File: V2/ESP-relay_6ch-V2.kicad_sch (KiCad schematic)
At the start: 103 parts, among them J1 24VDC, J2 24V INPUTS, J3 OUT1, J4 OUT1, J5 OUT1, J6 OUT1, J7 OUT1, J8 OUT1, K1 G5PZ-1A, K2 G5PZ-1A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

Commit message: footprint updates
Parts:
- C1, C2: symbol Device:CP1_Small -> Device:C_Polarized_Small_US
- U4, U5, U6, U7, U8, U9: footprint Tales:SMDIP-4_W9.53mm -> Package_DIP:SMDIP-4_W9.53mm
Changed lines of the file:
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@@
       (effects (font (size 1.27 1.27) italic) (justify left) hide)
     )
-    (property "Datasheet" "~" (id 3) (at 203.2 30.48 0)
+    (property "Datasheet" "http://www.st.com/content/ccc/resource/technical/document/datasheet/41/4f/b3/b0/12/d4/47/88/CD00000444.pdf/files/CD00000444.pdf/jcr:content/translations/en.CD00000444.pdf" (id 3) (at 203.2 30.48 0)
       (effects (font (size 1.27 1.27)) hide)
     )
@@
       (effects (font (size 1.27 1.27)) hide)
     )
-    (property "Datasheet" "~" (id 3) (at 312.42 72.39 0)
+    (property "Datasheet" "https://wiki.wemos.cc/products:d1:d1_mini#documentation" (id 3) (at 312.42 72.39 0)
       (effects (font (size 1.27 1.27)) hide)
     )
@@
       (effects (font (size 1.27 1.27)) (justify left) hide)
     )
-    (property "Datasheet" "~" (id 3) (at 349.25 93.98 0)
+    (property "Datasheet" "https://www.omron.com/ecb/products/pdf/en-g5q.pdf" (id 3) (at 349.25 93.98 0)
       (effects (font (size 1.27 1.27)) hide)
     )
@@
       (effects (font (size 1.27 1.27)) (justify left) hide)
     )
-    (property "Datasheet" "~" (id 3) (at 232.41 147.32 0)
+    (property "Datasheet" "https://www.omron.com/ecb/products/pdf/en-g5q.pdf" (id 3) (at 232.41 147.32 0)
       (effects (font (size 1.27 1.27)) hide)
     )
@@
       (effects (font (size 1.27 1.27)) (justify left) hide)
     )
-    (property "Datasheet" "~" (id 3) (at 349.25 147.32 0)
+    (property "Datasheet" "https://www.omron.com/ecb/products/pdf/en-g5q.pdf" (id 3) (at 349.25 147.32 0)
       (effects (font (size 1.27 1.27)) hide)
     )
@@
       (effects (font (size 1.27 1.27)) (justify left) hide)
     )
-    (property "Datasheet" "~" (id 3) (at 232.41 200.66 0)
+    (property "Datasheet" "https://www.omron.com/ecb/products/pdf/en-g5q.pdf" (id 3) (at 232.41 200.66 0)
       (effects (font (size 1.27 1.27)) hide)
     )
@@
       (effects (font (size 1.27 1.27)) (justify left) hide)
     )
-    (property "Datasheet" "~" (id 3) (at 349.25 200.66 0)
+    (property "Datasheet" "https://www.omron.com/ecb/products/pdf/en-g5q.pdf" (id 3) (at 349.25 200.66 0)
       (effects (font (size 1.27 1.27)) hide)
     )
@@
       (effects (font (size 1.27 1.27)) (justify left) hide)
     )
-    (property "Datasheet" "~" (id 3) (at 232.41 93.98 0)
+    (property "Datasheet" "https://www.omron.com/ecb/products/pdf/en-g5q.pdf" (id 3) (at 232.41 93.98 0)
       (effects (font (size 1.27 1.27)) hide)
     )
@@
     (pin "4")
   )
-  (symbol (lib_id "Device:CP1_Small") (at 48.26 71.12 0) (unit 1)
+  (symbol (lib_id "Device:C_Polarized_Small_US") (at 48.26 71.12 0) (unit 1)
     (in_bom yes) (on_board yes)
     (property "Reference" "C2" (id 0) (at 50.8 68.58 0)
@@
     (pin "1")
   )
-  (symbol (lib_id "Device:CP1_Small") (at 22.86 71.12 0) (unit 1)
+  (symbol (lib_id "Device:C_Polarized_Small_US") (at 22.86 71.12 0) (unit 1)
     (in_bom yes) (on_board yes)
     (property "Reference" "C1" (id 0) (at 25.4 68.58 0)
@@
     (property "Reference" "U6" (id 0) (at 120.65 151.13 0))
     (property "Value" "LTV-817S" (id 1) (at 120.65 153.67 0))
-    (property "Footprint" "Tales:SMDIP-4_W9.53mm" (id 2) (at 120.65 170.18 0)
+    (property "Footprint" "Package_DIP:SMDIP-4_W9.53mm" (id 2) (at 120.65 170.18 0)
       (effects (font (size 1.27 1.27)) hide)
     )
-    (property "Datasheet" "~" (id 3) (at 111.76 154.94 0)
+    (property "Datasheet" "http://www.us.liteon.com/downloads/LTV-817-827-847.PDF" (id 3) (at 111.76 154.94 0)
       (effects (font (size 1.27 1.27)) hide)
     )
@@
     (property "Reference" "U7" (id 0) (at 120.65 172.72 0))
     (property "Value" "LTV-817S" (id 1) (at 120.65 175.26 0))
-    (property "Footprint" "Tales:SMDIP-4_W9.53mm" (id 2) (at 120.65 191.77 0)
+    (property "Footprint" "Package_DIP:SMDIP-4_W9.53mm" (id 2) (at 120.65 191.77 0)
       (effects (font (size 1.27 1.27)) hide)
     )
-    (property "Datasheet" "~" (id 3) (at 111.76 176.53 0)
+    (property "Datasheet" "http://www.us.liteon.com/downloads/LTV-817-827-847.PDF" (id 3) (at 111.76 176.53 0)
       (effects (font (size 1.27 1.27)) hide)
     )
@@
     (property "Reference" "U5" (id 0) (at 120.65 129.54 0))
     (property "Value" "LTV-817S" (id 1) (at 120.65 132.08 0))
-    (property "Footprint" "Tales:SMDIP-4_W9.53mm" (id 2) (at 120.65 148.59 0)
+    (property "Footprint" "Package_DIP:SMDIP-4_W9.53mm" (id 2) (at 120.65 148.59 0)
       (effects (font (size 1.27 1.27)) hide)
     )
-    (property "Datasheet" "~" (id 3) (at 111.76 133.35 0)
+    (property "Datasheet" "http://www.us.liteon.com/downloads/LTV-817-827-847.PDF" (id 3) (at 111.76 133.35 0)
       (effects (font (size 1.27 1.27)) hide)
     )
@@
     (property "Reference" "U9" (id 0) (at 120.65 215.9 0))
     (property "Value" "LTV-817S" (id 1) (at 120.65 218.44 0))
-    (property "Footprint" "Tales:SMDIP-4_W9.53mm" (id 2) (at 120.65 234.95 0)
+    (property "Footprint" "Package_DIP:SMDIP-4_W9.53mm" (id 2) (at 120.65 234.95 0)
       (effects (font (size 1.27 1.27)) hide)
     )
-    (property "Datasheet" "~" (id 3) (at 111.76 219.71 0)
+    (property "Datasheet" "http://www.us.liteon.com/downloads/LTV-817-827-847.PDF" (id 3) (at 111.76 219.71 0)
       (effects (font (size 1.27 1.27)) hide)
     )
@@
   (symbol (lib_id "power:GNDREF") (at 176.53 49.53 0) (unit 1)
     (in_bom yes) (on_board yes)
-    (property "Reference" "#PWR?" (id 0) (at 176.53 55.88 0)
+    (property "Reference" "#PWR0108" (id 0) (at 176.53 55.88 0)
       (effects (font (size 1.27 1.27)) hide)
     )
@@
     (property "Reference" "U8" (id 0) (at 120.65 194.31 0))
     (property "Value" "LTV-817S" (id 1) (at 120.65 196.85 0))
-    (property "Footprint" "Tales:SMDIP-4_W9.53mm" (id 2) (at 120.65 213.36 0)
+    (property "Footprint" "Package_DIP:SMDIP-4_W9.53mm" (id 2) (at 120.65 213.36 0)
       (effects (font (size 1.27 1.27)) hide)
     )
-    (property "Datasheet" "~" (id 3) (at 111.76 198.12 0)
+    (property "Datasheet" "http://www.us.liteon.com/downloads/LTV-817-827-847.PDF" (id 3) (at 111.76 198.12 0)
       (effects (font (size 1.27 1.27)) hide)
     )
@@
     (property "Reference" "U4" (id 0) (at 120.65 107.95 0))
     (property "Value" "LTV-817S" (id 1) (at 120.65 110.49 0))
-    (property "Footprint" "Tales:SMDIP-4_W9.53mm" (id 2) (at 120.65 127 0)
+    (property "Footprint" "Package_DIP:SMDIP-4_W9.53mm" (id 2) (at 120.65 127 0)
       (effects (font (size 1.27 1.27)) hide)
     )
-    (property "Datasheet" "~" (id 3) (at 111.76 111.76 0)
+    (property "Datasheet" "http://www.us.liteon.com/downloads/LTV-817-827-847.PDF" (id 3) (at 111.76 111.76 0)
       (effects (font (size 1.27 1.27)) hide)
     )
@@
     )
     (path "/9385be33-d48d-4257-8c07-24842288edd5"
-      (reference "#PWR?") (unit 1) (value "GNDREF") (footprint "")
+      (reference "#PWR0108") (unit 1) (value "GNDREF") (footprint "")
     )
     (path "/00000000-0000-0000-0000-000062418b8f"
@@
     )
     (path "/e41c8ba8-d546-4f8b-b36a-c7995cebe79c"
-      (reference "U4") (unit 1) (value "LTV-817S") (footprint "Tales:SMDIP-4_W9.53mm")
+      (reference "U4") (unit 1) (value "LTV-817S") (footprint "Package_DIP:SMDIP-4_W9.53mm")
     )
     (path "/6ba5bf41-6e66-42b1-83b1-2c70a4b4c2de"
-      (reference "U5") (unit 1) (value "LTV-817S") (footprint "Tales:SMDIP-4_W9.53mm")
+      (reference "U5") (unit 1) (value "LTV-817S") (footprint "Package_DIP:SMDIP-4_W9.53mm")
     )
     (path "/290fdcc5-3b98-44d5-b0bc-e642d931fb96"
-      (reference "U6") (unit 1) (value "LTV-817S") (footprint "Tales:SMDIP-4_W9.53mm")
+      (reference "U6") (unit 1) (value "LTV-817S") (footprint "Package_DIP:SMDIP-4_W9.53mm")
     )
     (path "/518902cd-4835-4abd-b184-bfbf5192b239"
-      (reference "U7") (unit 1) (value "LTV-817S") (footprint "Tales:SMDIP-4_W9.53mm")
+      (reference "U7") (unit 1) (value "LTV-817S") (footprint "Package_DIP:SMDIP-4_W9.53mm")
     )
     (path "/cc3468d2-c4c5-46a1-b8d8-a0ff0eede2e1"
-      (reference "U8") (unit 1) (value "LTV-817S") (footprint "Tales:SMDIP-4_W9.53mm")
+      (reference "U8") (unit 1) (value "LTV-817S") (footprint "Package_DIP:SMDIP-4_W9.53mm")
     )
     (path "/789ed84c-79d1-421a-acdb-4fbcb6c37ec2"
-      (reference "U9") (unit 1) (value "LTV-817S") (footprint "Tales:SMDIP-4_W9.53mm")
+      (reference "U9") (unit 1) (value "LTV-817S") (footprint "Package_DIP:SMDIP-4_W9.53mm")
     )
   )

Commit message: work in progress
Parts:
- removed J1: 24VDC, Tales:TerminalBlock_Phoenix_MKDS-3-2-5.08_1x02_P5.08mm_Horizontal, symbol Connector_Generic:Conn_01x02
- D10, D5, D6, D7, D8, D9: JLCPCB BOM 0 -> 1; LCSC Part (none) -> C109072; Mfr Rectron -> Semtech; Vendor Mouser -> JLCPCB; Vendor PN 583-ZMM5239B -> C109072
- J1: renamed from J2; value 24V INPUTS -> POWER & INPUTS; footprint Tales:TerminalBlock_Phoenix_MKDS-3-6-5.08_1x06_P5.08mm_Horizontal -> Tales:TerminalBlock_Phoenix_MKDS-3-8-5.08_1x08_P5.08mm_Horizontal; symbol Connector_Generic:Conn_01x06 -> Connector_Generic:Conn_01x08
- renumbered J3 to J2, J4 to J3, J5 to J4, J6 to J5, J7 to J6, J8 to J7
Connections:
- net +24V: now also J1.1 (Pin_1)
- net GNDREF: now also J1.2 (Pin_2)
- net at R4.2: now also J1.3 (Pin_3); no longer J1.1 (Pin_1)
- net at R6.2: now also J1.4 (Pin_4); no longer J1.2 (Pin_2)
- net at R8.2: now also J1.5 (Pin_5); no longer J1.3 (Pin_3)
- net at R10.2: now also J1.6 (Pin_6); no longer J1.4 (Pin_4)
- net at R12.2: now also J1.7 (Pin_7); no longer J1.5 (Pin_5)
- net at R14.2: now also J1.8 (Pin_8); no longer J1.6 (Pin_6)
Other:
- moved on the sheet: C1, C2, C3, D1, D2, D23, D24, D3, D4, R1, R2, R28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

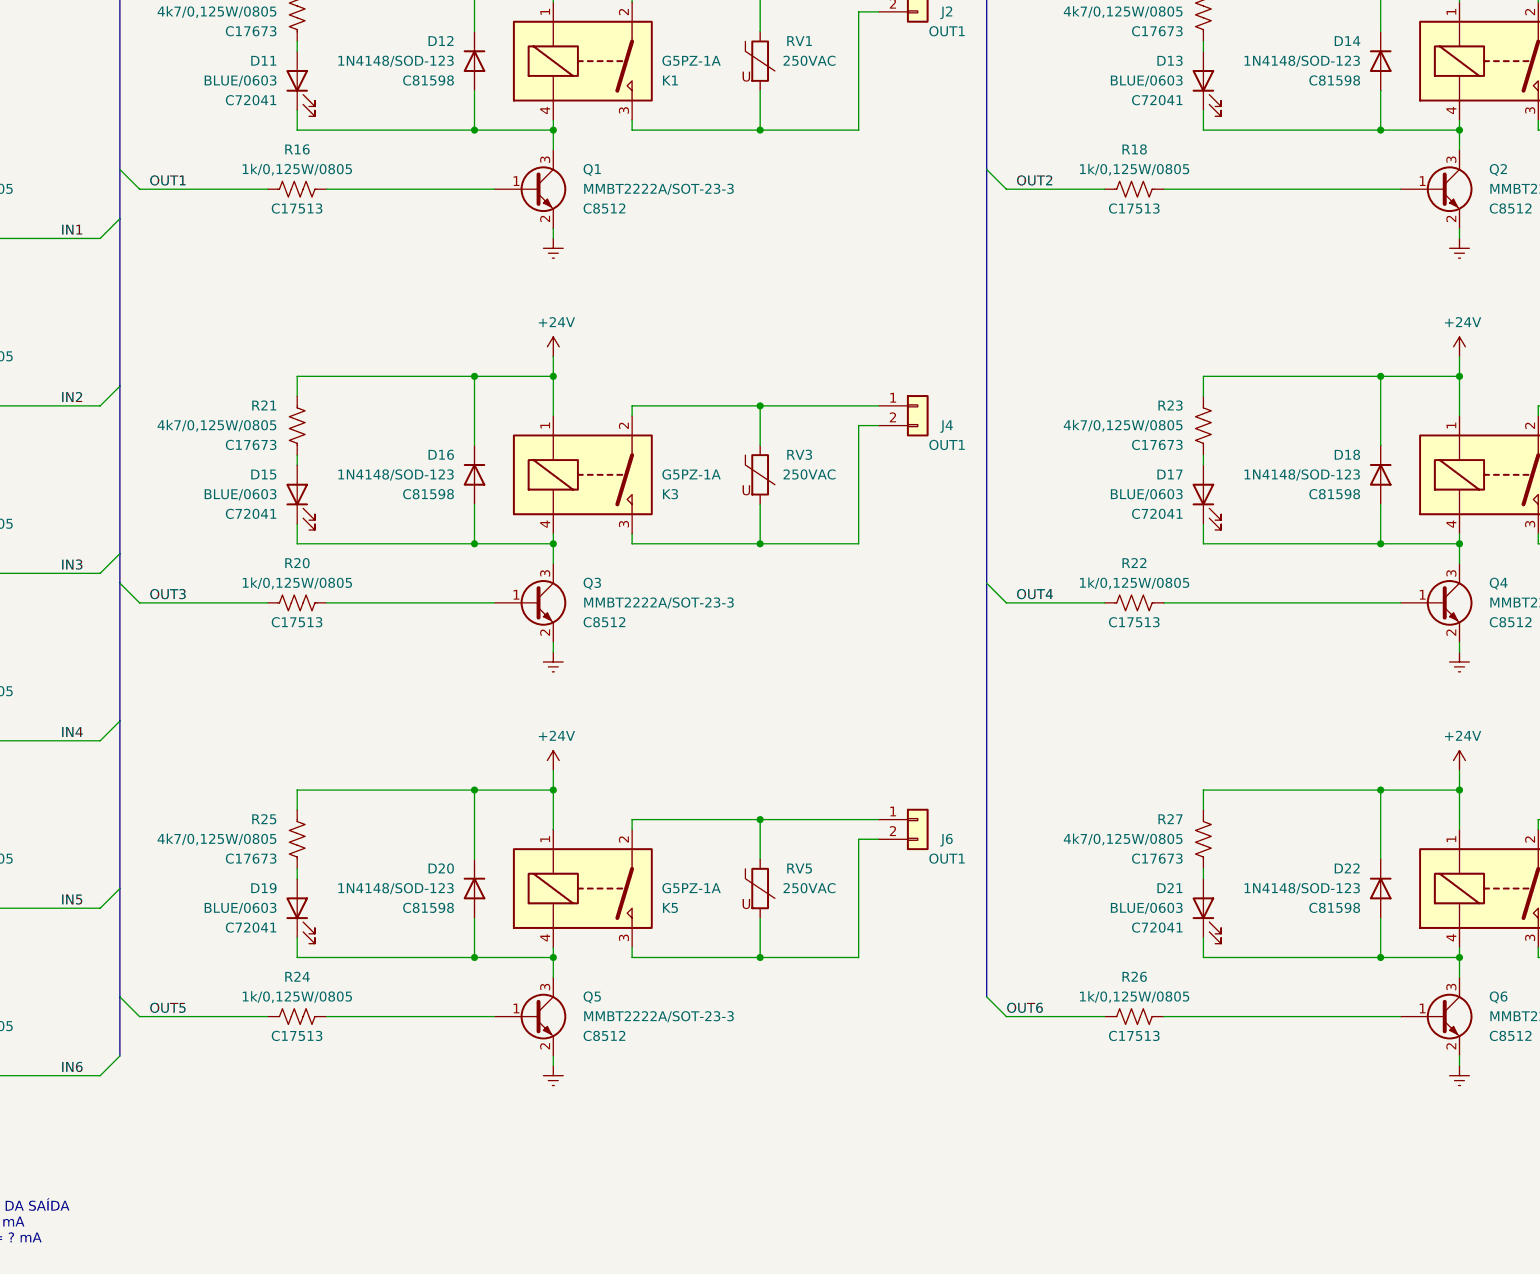
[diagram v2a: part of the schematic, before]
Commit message: add pull down resistors
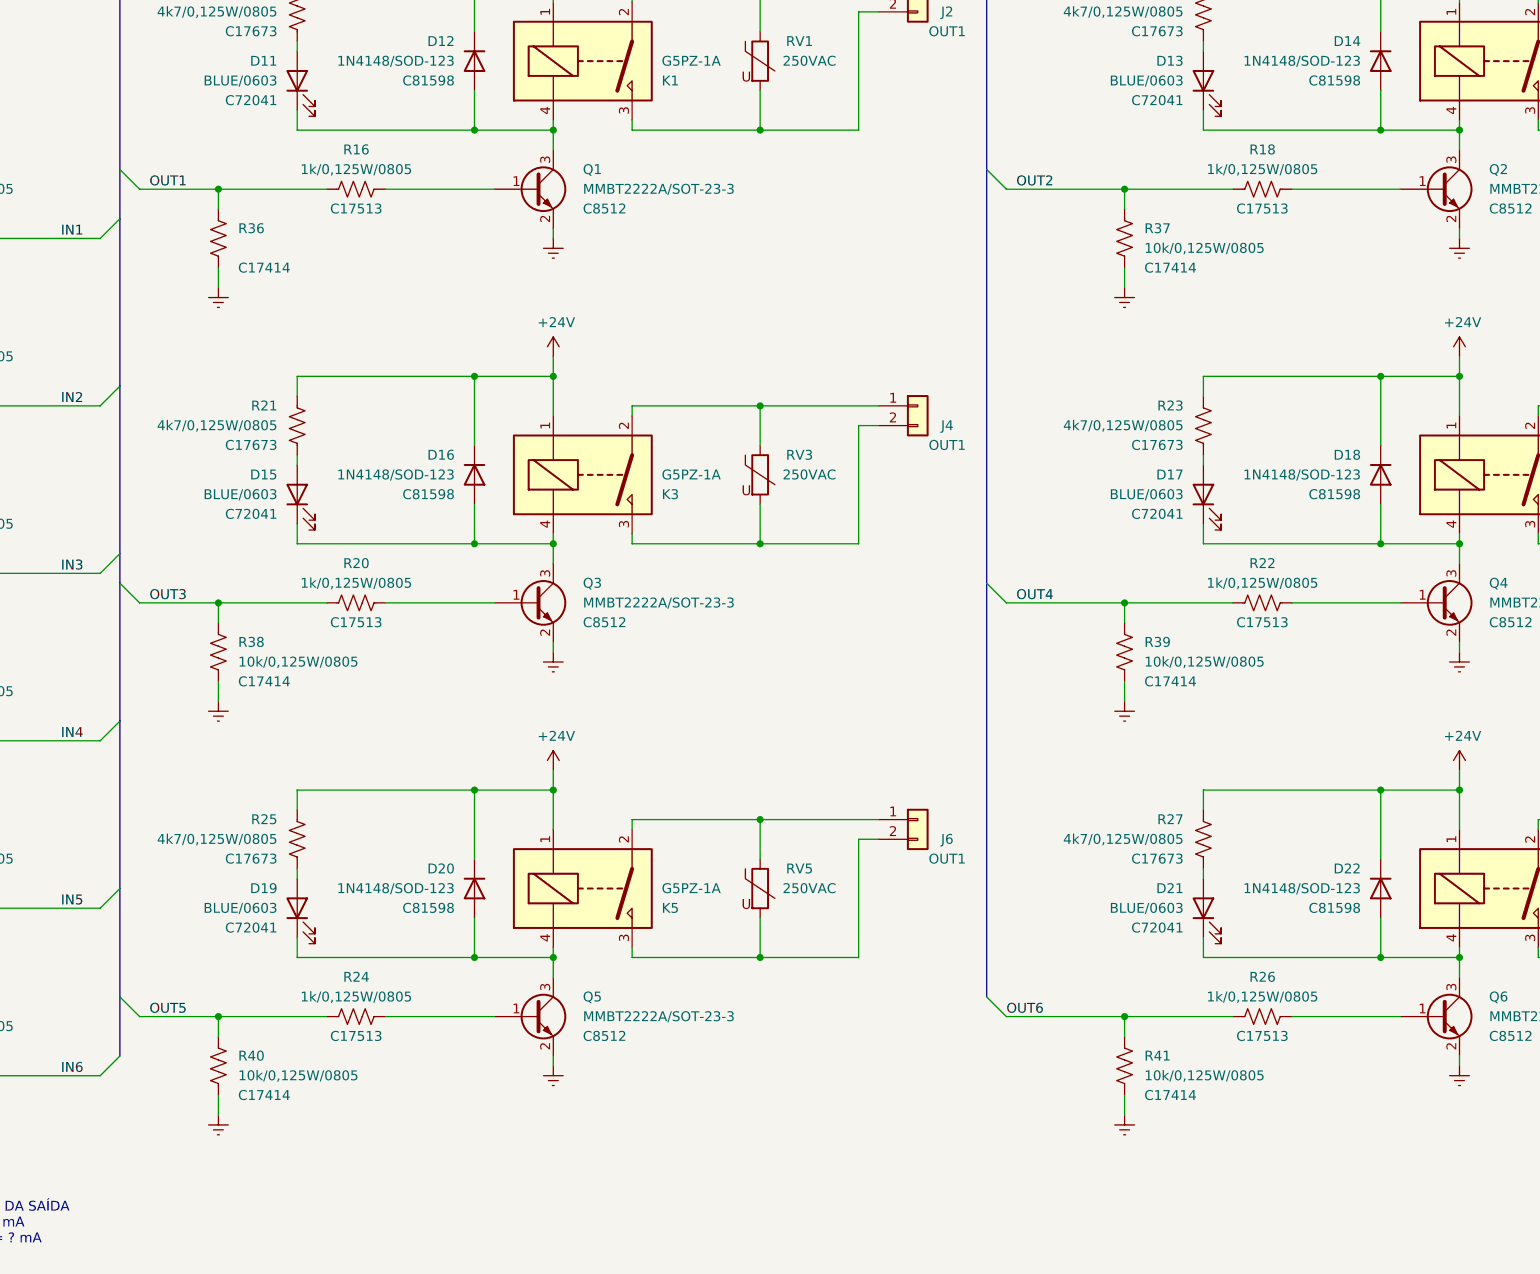
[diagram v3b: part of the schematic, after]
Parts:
- added R36: (no value), Tales:R_0805_2012Metric, symbol Device:R_US
- added R37, R38, R39, R40, R41: 10k/0,125W/0805, Tales:R_0805_2012Metric, symbol Device:R_US
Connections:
- net 32-GPIO13: now also R39.1
- net 32-GPIO16: now also R38.1
- net 32-GPIO2: now also R40.1
- net 32-GPIO32: now also R37.1
- net 32-GPIO33: now also R36.1
- net 32-GPIO4: now also R41.1
- net GNDREF: now also R36.2, R37.2, R38.2, R39.2, R40.2, R41.2
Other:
- moved on the sheet: R16, R18, R20, R22, R24, R26

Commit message: Updates
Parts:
- added R42: (no value), Tales:R_0805_2012Metric, symbol Device:R_US
- R36: value (none) -> 10k/0,125W/0805
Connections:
- net +3V3: now also R42.1
- net at U2.4 (ESP_EN): now also U3.1 (~{RST}), R42.2
- net 32-GPI34 renamed IN4
- net 32-GPI35 renamed IN3
- net 32-GPI36 renamed IN2
- net 32-GPI39 renamed IN1
- net 32-GPIO13 renamed OUT4
- net 32-GPIO14 renamed IN6
- net 32-GPIO15 renamed IN5
- net 32-GPIO16 renamed OUT3
- net 32-GPIO2 renamed OUT5
- net 32-GPIO32 renamed OUT2
- net 32-GPIO33 renamed OUT1
- net 32-GPIO4 renamed OUT6
- no-connect marks 10 -> 8
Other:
- moved on the sheet: C1, C2, C3, C4, C5, C6, C7, C8, C9, D1, D10, D11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

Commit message: PCB tweaks
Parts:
- C1: value 47uF/35V/6,3x5,4 -> (none); footprint Tales:CP_Elec_6.3x5.4 -> (none)
- C2: value 0,33uF/35V -> (none); footprint Tales:CP_EIA-3216-18_Kemet-A_Pad1.58x1.35mm_HandSolder -> (none)
- C3: value 0,1uF/50V/0805 -> (none); footprint Tales:C_0805_2012Metric -> (none)
- C4, C5, C6, C7, C8, C9: value 33nF/50V/0805 -> (none); footprint Tales:C_0805_2012Metric -> (none)
- D1: value SM4007PL/SOD-123 -> (none); footprint Tales:D_SOD-123 -> (none)
- D10, D5, D6, D7, D8, D9: value 9V1/500mW -> (none); footprint Tales:D_MiniMELF -> (none)
- D11, D13, D15, D17, D19, D21: value BLUE/0603 -> (none); footprint Tales:LED_0603_1608Metric -> (none)
- D12, D14, D16, D18, D20, D22: value 1N4148/SOD-123 -> (none); footprint Tales:D_SOD-123 -> (none)
- D2, D3, D4: value GREEN/0603 -> (none); footprint Tales:LED_0603_1608Metric -> (none)
- D23, D24: value 7V5/5W/SMB -> (none); footprint Tales:D_SMB -> (none)
- J1: value POWER & INPUTS -> (none); footprint Tales:TerminalBlock_Phoenix_MKDS-3-8-5.08_1x08_P5.08mm_Horizontal -> (none)
- J2, J3, J4, J5, J6, J7: value OUT1 -> (none); footprint Tales:TerminalBlock_Phoenix_MKDS-3-2-5.08_1x02_P5.08mm_Horizontal -> (none)
- K1, K2, K3, K4, K5, K6: value G5PZ-1A -> (none); footprint Tales:Relay_SPST_Omron-G5PZ-1A -> (none)
- Q1, Q2, Q3, Q4, Q5, Q6: value MMBT2222A/SOT-23-3 -> (none); footprint Tales:SOT-23 -> (none)
- R1: value 270R/0,125W/0805 -> (none); footprint Tales:R_0805_2012Metric -> (none)
- R10, R12, R14, R4, R6, R8: value 1k2/0,125W/0805 -> (none); footprint Tales:R_0805_2012Metric -> (none)
- R11, R13, R15, R5, R7, R9: value 3k3/0,125W/0805 -> (none); footprint Tales:R_0805_2012Metric -> (none)
- R16, R18, R20, R22, R24, R26: value 1k/0,125W/0805 -> (none); footprint Tales:R_0805_2012Metric -> (none)
- R17, R19, R21, R23, R25, R27: value 4k7/0,125W/0805 -> (none); footprint Tales:R_0805_2012Metric -> (none)
- R2: value 3k9/0,125W/0805 -> (none); footprint Tales:R_0805_2012Metric -> (none)
- R28, R29, R30, R31, R32, R33, R34, R35: value 56R/0,125W/0805 -> (none); footprint Tales:R_0805_2012Metric -> (none)
- R3: value 680R/0,125W/0805 -> (none); footprint Tales:R_0805_2012Metric -> (none)
- R36, R37, R38, R39, R40, R41: value 10k/0,125W/0805 -> (none); footprint Tales:R_0805_2012Metric -> (none)
- R42: footprint Tales:R_0805_2012Metric -> (none)
- RV1, RV2, RV3, RV4, RV5, RV6: value 250VAC -> (none); footprint Tales:RV_Disc_D12mm_W3.9mm_P7.5mm -> (none)
- U1: value L78M05/TO-252-2 -> (none); footprint Tales:TO-252-2 -> (none)
- U2: value Olimex_ESP32-POE -> (none); footprint Tales:Olimex_ESP32-POE_Pads -> (none)
- U3: value WeMos_D1_mini -> (none); footprint Tales:WEMOS_D1_mini_light_pads -> (none)
- U4, U5, U6, U7, U8, U9: value LTV-817S -> (none); footprint Package_DIP:SMDIP-4_W9.53mm -> (none)
